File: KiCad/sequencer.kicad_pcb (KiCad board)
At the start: 2 copper layers, 79.9 x 100 mm, 126 parts, among them J1 CLOCK OUT, J2 GATE OUT, J3 CLOCK IN, J4 CV OUT, J5 RESET, J6 10-pin power header, Q1 BC848W, Q2 MMBT3904, Q3 MMBT3904, Q4 MMBT3904, Q5 MMBT3904, Q6 MMBT3904, Q7 MMBT3904, Q8 MMBT3904, Q9 MMBT3904, SW1 SW_Nidec_CAS-120A1, U1 TL074, U3 CD4017BE

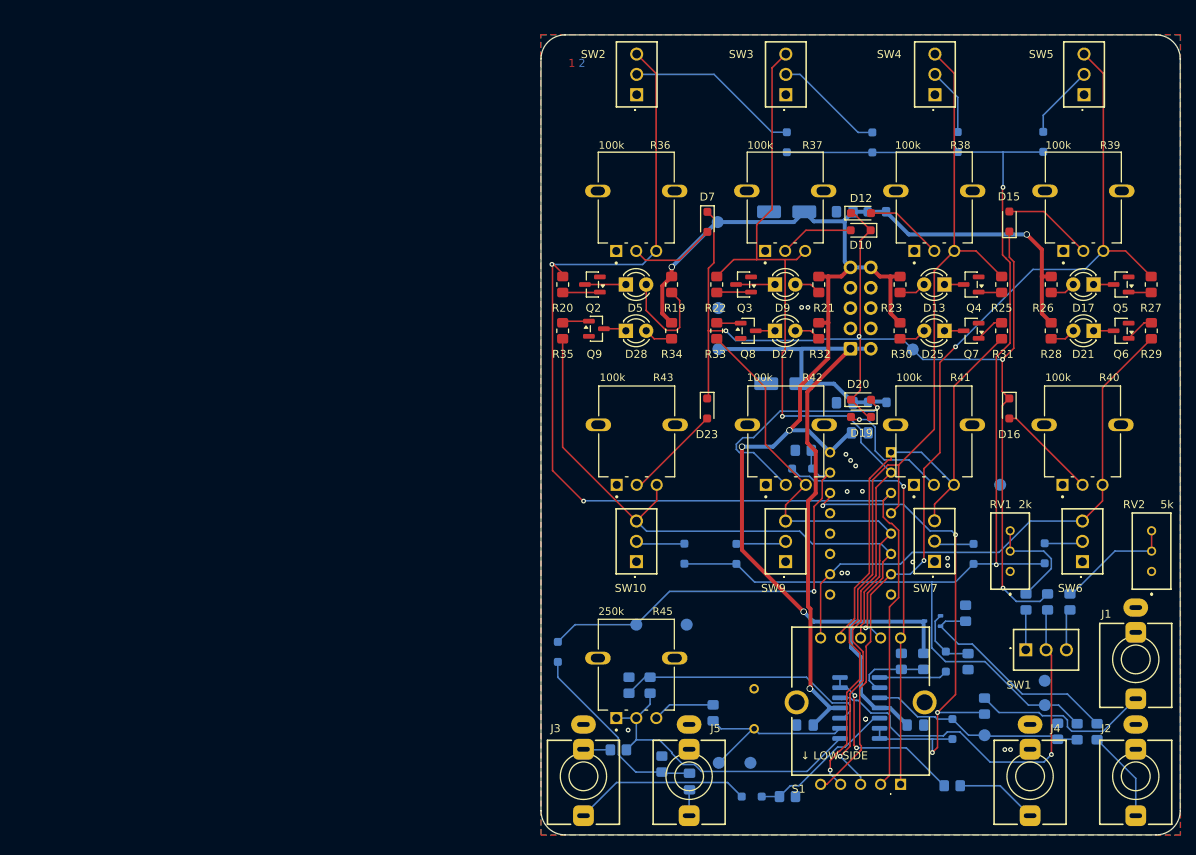
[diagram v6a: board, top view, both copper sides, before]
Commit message: fixing drc errors; mirroring potentiometers in sch due to error; mirroring switches on pcb
to do: change symbol description potentiometer (cw, ccw)
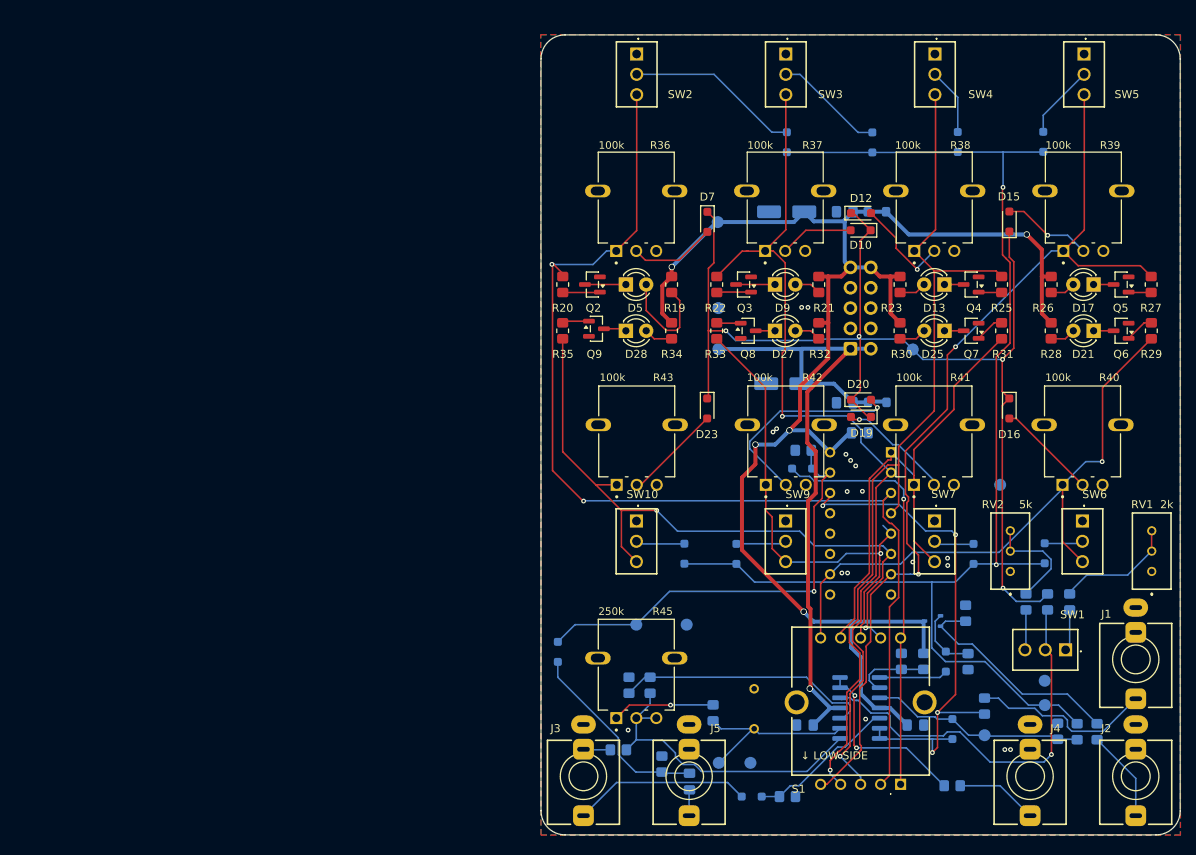
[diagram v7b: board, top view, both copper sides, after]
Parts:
- removed REF**: LayerMarker_2_3.81x2.54mm_TextH1mm_P1.27mm, Symbol:LayerMarker_2_3.81x2.54mm_TextH1mm_P1.27mm
- moved RV1 17.7 mm to (186.0, 108.7)
- moved RV2 17.7 mm to (168.3, 108.7)
- moved R14 5.49 mm to (170.3, 112.5)
- moved R13 5.45 mm to (175.7, 112.5)
- moved SW2 5.09 mm to (121.6, 44.0), turned to 180 degrees
- moved SW3 5.09 mm to (140.3, 44.0), turned to 180 degrees
- moved SW4 5.09 mm to (158.9, 44.0), turned to 180 degrees
- moved SW5 5.09 mm to (177.5, 44.0), turned to 180 degrees
- moved SW10 5.09 mm to (121.6, 102.4), turned to 180 degrees
- moved SW6 5.09 mm to (177.3, 102.4), turned to 180 degrees
- moved SW9 5.09 mm to (140.2, 102.4), turned to 180 degrees
- moved SW7 5.05 mm to (158.9, 102.4), turned to 180 degrees
- moved SW1 4.98 mm to (175.2, 118.5), turned to 90 degrees
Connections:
- R36 pad 1: GND -> /CD4017BE/Count0
- R36 pad 3: /CD4017BE/Count0 -> GND
- R37 pad 1: GND -> /CD4017BE/Count1
- R37 pad 3: /CD4017BE/Count1 -> GND
- R38 pad 1: GND -> /CD4017BE/Count2
- R38 pad 3: /CD4017BE/Count2 -> GND
- R39 pad 1: GND -> /CD4017BE/Count3
- R39 pad 3: /CD4017BE/Count3 -> GND
- R40 pad 1: GND -> /CD4017BE/Count4
- R40 pad 3: /CD4017BE/Count4 -> GND
- R41 pad 1: GND -> /CD4017BE/Count5
- R41 pad 3: /CD4017BE/Count5 -> GND
- R42 pad 1: GND -> /CD4017BE/Count6
- R42 pad 3: /CD4017BE/Count6 -> GND
- R43 pad 1: GND -> /CD4017BE/Count7
- R43 pad 3: /CD4017BE/Count7 -> GND
- R45 pad 1: Net-(R16-Pad2) -> Net-(R15-Pad1)
- R45 pad 3: Net-(R15-Pad1) -> Net-(R16-Pad2)
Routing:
- net /CD4017BE/Count0: track 150.4 -> 140.4 mm
- net /CD4017BE/Count1: track 120.6 -> 111.9 mm
- net /CD4017BE/Count4: track 69.1 -> 77.1 mm, vias 0 -> 1
- net Net-(R15-Pad1): track 7.78 -> 12.9 mm, vias 0 -> 1
- net /CD4017BE/Count7: track 78.7 -> 83.2 mm, vias 1 -> 2
- net /CD4017BE/Count2: track 114.9 -> 111.3 mm
- net Net-(D20-A): track 29.5 -> 26.3 mm
- net /CD4017BE/Count6: track 56.9 -> 59.9 mm, vias 0 -> 1
- net /CD4017BE/Count5: track 61.8 -> 64.7 mm
- net /CD4017BE/Count3: track 120.1 -> 117.3 mm
- net Net-(D12-A): track 9.86 -> 12.6 mm, vias 0 -> 1
- net Net-(R13-Pad1): track 13.8 -> 15.5 mm
- net Net-(D19-A): track 15.6 -> 14.2 mm
- net +12V: track 193.7 -> 192.9 mm
- net Net-(SW1-C): track 5.00 -> 5.82 mm
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
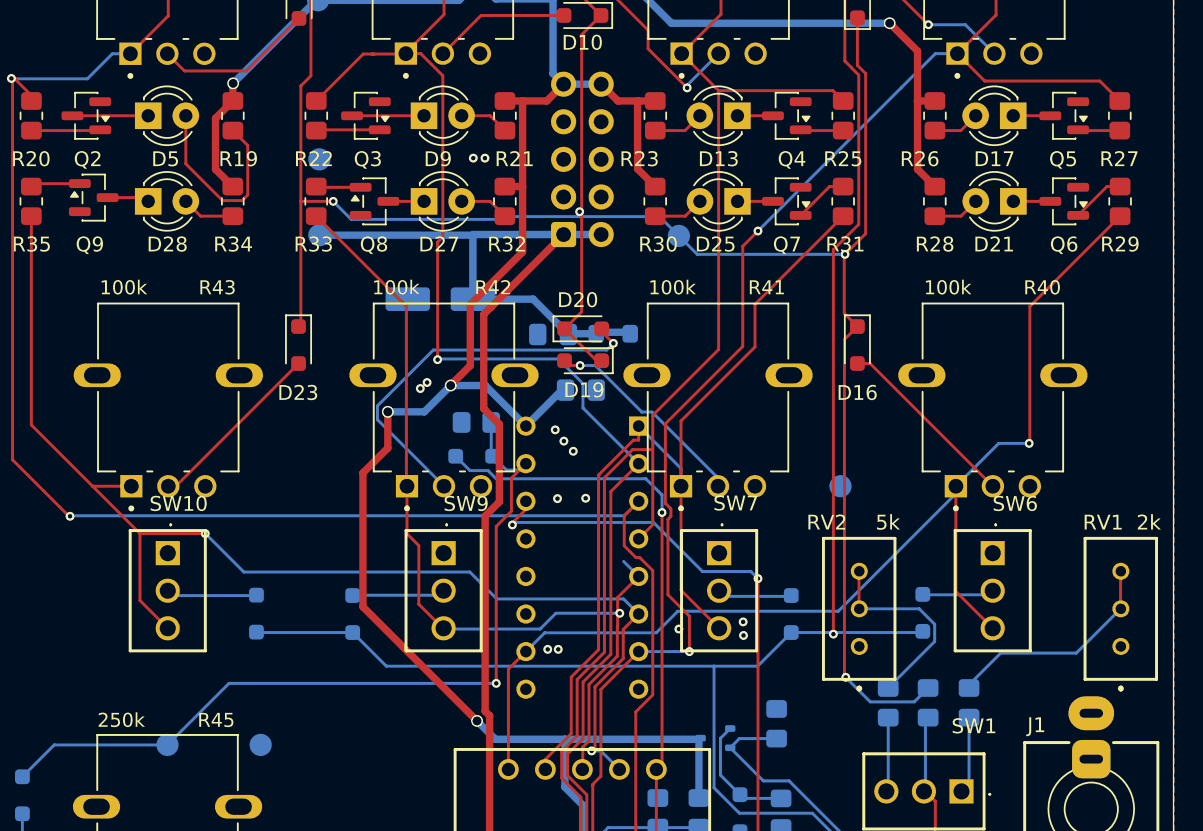
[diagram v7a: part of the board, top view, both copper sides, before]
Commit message: placing logos
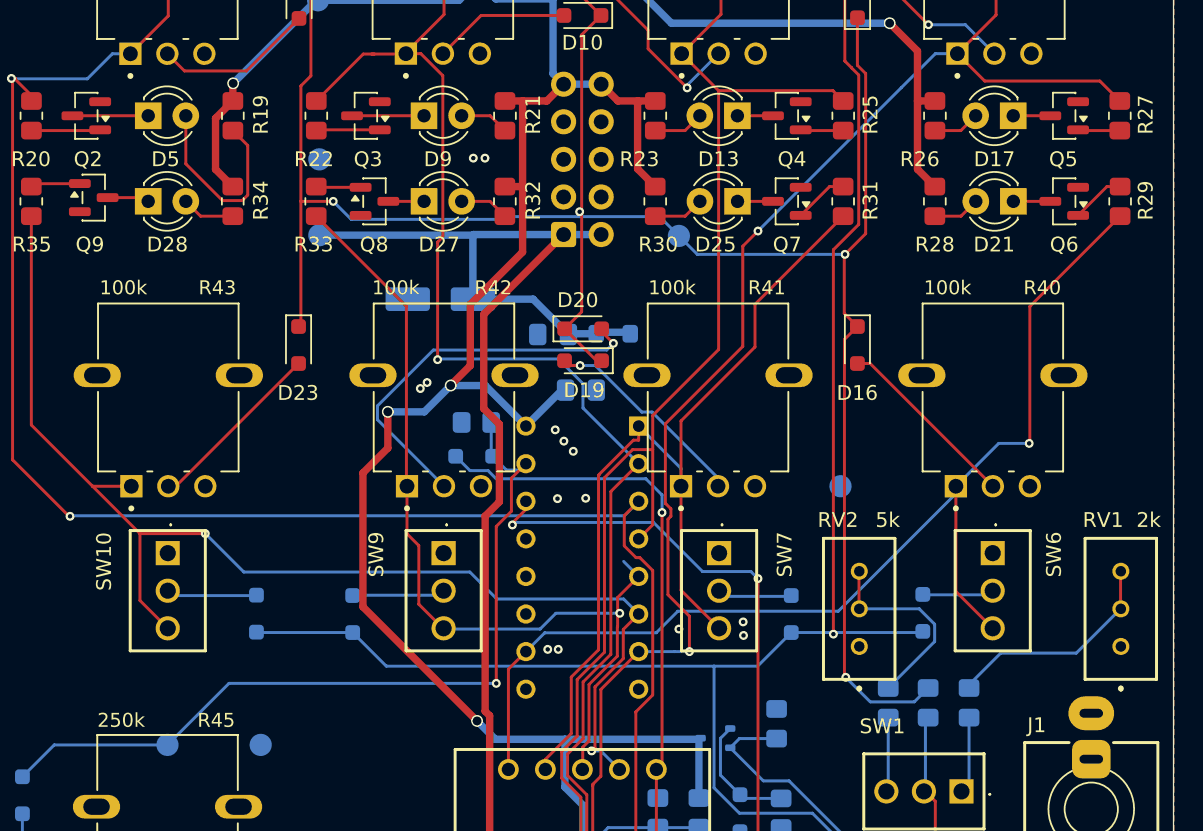
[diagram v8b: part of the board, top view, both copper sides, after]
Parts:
- added G***: LOGO, LOGO, B.Cu at (171.4, 79.0)
- added G***: LOGO, LOGO, B.Cu at (171.9, 85.7)
